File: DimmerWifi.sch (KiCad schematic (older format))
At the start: 13 parts, among them J1 AC, J2 Load, J3 Conn_01x04, U1 MOC3021M, U2 4N25

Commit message: fix
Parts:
- removed D1: Q_TRIAC_AAG, TO_SOT_Packages_THT:TO-220-3_Vertical, symbol Q_TRIAC_AAG
- removed D3: LED, LEDs:LED_D5.0mm, symbol LED
- added Q1: TRIAC_BTA, w_to:to220, symbol TRIAC_BTA
- J1, J2: footprint TerminalBlocks_Phoenix:TerminalBlock_Phoenix_MPT-2.54mm_2pol -> w_conn_mkds:mkds_1,5-2
- J3: footprint Pin_Headers:Pin_Header_Angled_1x04_Pitch2.54mm -> w_pin_strip:pin_strip_2mm_4
- R1, R2, R3, R4, R5: footprint Resistors_THT:R_Axial_DIN0411_L9.9mm_D3.6mm_P7.62mm_Vertical -> w_pth_resistors:RC03
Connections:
- net Fase: now also Q1.2 (A2)
- net at U1.4: now also Q1.1 (G)
- net at J2.1 (Pin_1), R3.1: now also Q1.3 (A1)
- net at R4.2: now also J3.4 (Pin_4)
- net +3.3V renamed +3V3
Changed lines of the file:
@@
 EESchema Schematic File Version 2
+LIBS:DimmerWifi-rescue
 LIBS:power
 LIBS:device
@@
 LIBS:contrib
 LIBS:valves
+LIBS:w_analog
+LIBS:w_connectors
+LIBS:w_device
+LIBS:w_logic
+LIBS:w_memory
+LIBS:w_microcontrollers
+LIBS:w_opto
+LIBS:w_relay
+LIBS:w_rtx
+LIBS:w_transistor
+LIBS:w_vacuum
+LIBS:DimmerWifi-cache
 EELAYER 25 0
 EELAYER END
@@
 F 0 "R1" V 2680 2000 50  0000 C CNN
 F 1 "30k" V 2600 2000 50  0000 C CNN
-F 2 "Resistors_THT:R_Axial_DIN0411_L9.9mm_D3.6mm_P7.62mm_Vertical" V 2530 2000 50  0001 C CNN
+F 2 "w_pth_resistors:RC03" V 2530 2000 50  0001 C CNN
 F 3 "" H 2600 2000 50  0001 C CNN
 	1    2600 2000
@@
 F 0 "R2" V 2680 2600 50  0000 C CNN
 F 1 "30k" V 2600 2600 50  0000 C CNN
-F 2 "Resistors_THT:R_Axial_DIN0411_L9.9mm_D3.6mm_P7.62mm_Vertical" V 2530 2600 50  0001 C CNN
+F 2 "w_pth_resistors:RC03" V 2530 2600 50  0001 C CNN
 F 3 "" H 2600 2600 50  0001 C CNN
 	1    2600 2600
@@
 F 0 "R5" V 4680 2200 50  0000 C CNN
 F 1 "3.3k" V 4600 2200 50  0000 C CNN
-F 2 "Resistors_THT:R_Axial_DIN0411_L9.9mm_D3.6mm_P7.62mm_Vertical" V 4530 2200 50  0001 C CNN
+F 2 "w_pth_resistors:RC03" V 4530 2200 50  0001 C CNN
 F 3 "" H 4600 2200 50  0001 C CNN
 	1    4600 2200
@@
 F 0 "J2" H 1500 2850 50  0000 C CNN
 F 1 "Load" H 1500 2550 50  0000 C CNN
-F 2 "TerminalBlocks_Phoenix:TerminalBlock_Phoenix_MPT-2.54mm_2pol" H 1500 2750 50  0001 C CNN
+F 2 "w_conn_mkds:mkds_1,5-2" H 1500 2750 50  0001 C CNN
 F 3 "" H 1500 2750 50  0001 C CNN
 	1    1500 2750
@@
 	1700 2300 2350 2300
 $Comp
-L +3.3V #PWR01
+L +3.3V-RESCUE-DimmerWifi #PWR01
 U 1 1 59F65F9C
 P 4600 1950
@@
 	4600 1950 4600 2050
 $Comp
-L GND #PWR02
+L GND-RESCUE-DimmerWifi #PWR02
 U 1 1 59F65FE8
 P 4550 2600
@@
 F 0 "R4" V 3780 3350 50  0000 C CNN
 F 1 "180" V 3700 3350 50  0000 C CNN
-F 2 "Resistors_THT:R_Axial_DIN0411_L9.9mm_D3.6mm_P7.62mm_Vertical" V 3630 3350 50  0001 C CNN
+F 2 "w_pth_resistors:RC03" V 3630 3350 50  0001 C CNN
 F 3 "" H 3700 3350 50  0001 C CNN
 	1    3700 3350
@@
 	3550 3350 3450 3350
 $Comp
-L GND #PWR03
+L GND-RESCUE-DimmerWifi #PWR03
 U 1 1 59F66456
 P 3500 3100
@@
 	3500 3150 3500 3100
 $Comp
-L Q_TRIAC_AAG D1
-U 1 1 59F664AA
-P 2250 3200
-F 0 "D1" H 2375 3225 50  0000 L CNN
-F 1 "Q_TRIAC_AAG" H 2375 3150 50  0000 L CNN
-F 2 "TO_SOT_Packages_THT:TO-220-3_Vertical" V 2325 3225 50  0001 C CNN
-F 3 "" V 2250 3200 50  0001 C CNN
-	1    2250 3200
-	-1   0    0    1
-$EndComp
-$Comp
 L R R3
 U 1 1 59F66521
@@
 F 0 "R3" V 2680 3350 50  0000 C CNN
 F 1 "1k" V 2600 3350 50  0000 C CNN
-F 2 "Resistors_THT:R_Axial_DIN0411_L9.9mm_D3.6mm_P7.62mm_Vertical" V 2530 3350 50  0001 C CNN
+F 2 "w_pth_resistors:RC03" V 2530 3350 50  0001 C CNN
 F 3 "" H 2600 3350 50  0001 C CNN
 	1    2600 3350
@@
 	1750 3350 2450 3350
 Wire Wire Line
-	2400 3100 2650 3100
+	2300 3100 2650 3100
 Wire Wire Line
 	2650 3100 2650 3150
@@
 F 0 "J1" H 1500 2400 50  0000 C CNN
 F 1 "AC" H 1500 2100 50  0000 C CNN
-F 2 "TerminalBlocks_Phoenix:TerminalBlock_Phoenix_MPT-2.54mm_2pol" H 1500 2300 50  0001 C CNN
+F 2 "w_conn_mkds:mkds_1,5-2" H 1500 2300 50  0001 C CNN
 F 3 "" H 1500 2300 50  0001 C CNN
 	1    1500 2300
@@
 Neutro
 Wire Wire Line
-	2250 3050 2250 2200
-Connection ~ 2250 2200
-Wire Wire Line
 	1700 2650 1750 2650
 Wire Wire Line
@@
 Wire Wire Line
 	1750 2750 1750 3350
-Connection ~ 2250 3350
 Wire Wire Line
 	2350 2000 2450 2000
@@
 F 0 "J3" H 5800 2550 50  0000 C CNN
 F 1 "Conn_01x04" H 5800 2050 50  0000 C CNN
-F 2 "Pin_Headers:Pin_Header_Angled_1x04_Pitch2.54mm" H 5800 2350 50  0001 C CNN
+F 2 "w_pin_strip:pin_strip_2mm_4" H 5800 2350 50  0001 C CNN
 F 3 "" H 5800 2350 50  0001 C CNN
 	1    5800 2350
@@
 	5600 2550 5400 2550
 Wire Wire Line
-	5400 2550 5400 3350
+	5400 3350 5400 2550
 Wire Wire Line
 	4550 2600 4550 2500
 Connection ~ 4550 2500
-$Comp
-L LED D3
-U 1 1 59F678D1
-P 4100 3350
-F 0 "D3" H 4100 3450 50  0000 C CNN
-F 1 "LED" H 4100 3250 50  0000 C CNN
-F 2 "LEDs:LED_D5.0mm" H 4100 3350 50  0001 C CNN
-F 3 "" H 4100 3350 50  0001 C CNN
-	1    4100 3350
-	1    0    0    -1
-$EndComp
-Wire Wire Line
-	3950 3350 3850 3350
-Wire Wire Line
-	5400 3350 4250 3350
+Wire Wire Line
+	3850 3350 5400 3350
 $Comp
 L PWR_FLAG #FLG04
@@
 Connection ~ 5400 2000
 NoConn ~ 4450 2300
+$Comp
+L TRIAC_BTA Q1
+U 1 1 59F8B5BD
+P 2100 3000
+F 0 "Q1" H 2200 3150 60  0000 C CNN
+F 1 "TRIAC_BTA" H 2400 2750 60  0000 C CNN
+F 2 "w_to:to220" H 2100 3000 60  0001 C CNN
+F 3 "" H 2100 3000 60  0000 C CNN
+	1    2100 3000
+	1    0    0    -1
+$EndComp
+Wire Wire Line
+	2100 2850 2100 2200
+Connection ~ 2100 2200
+Wire Wire Line
+	2100 3150 2100 3350
+Connection ~ 2100 3350
 $EndSCHEMATC

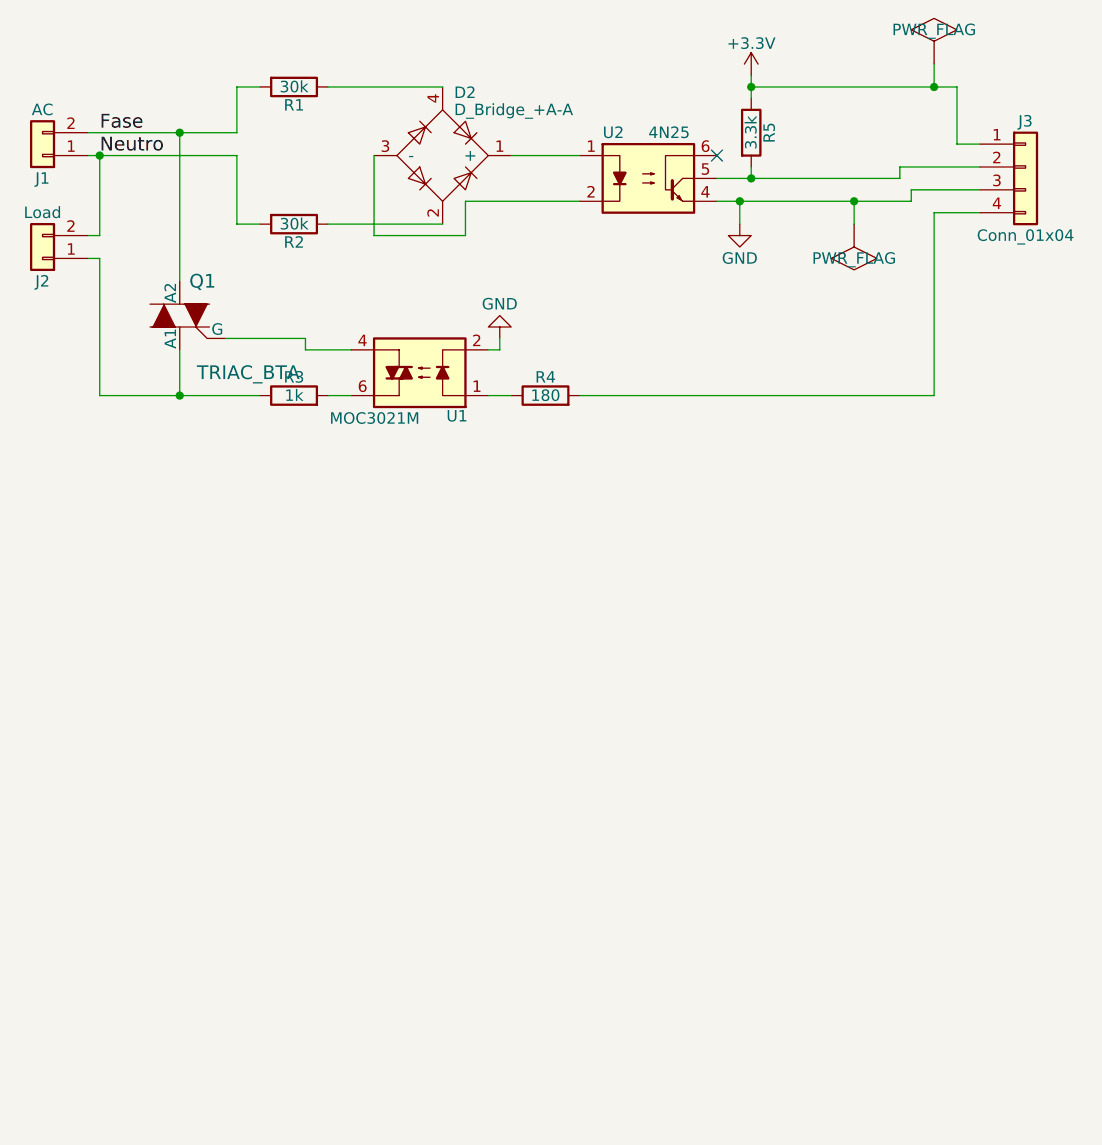
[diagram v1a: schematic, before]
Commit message: add esp32
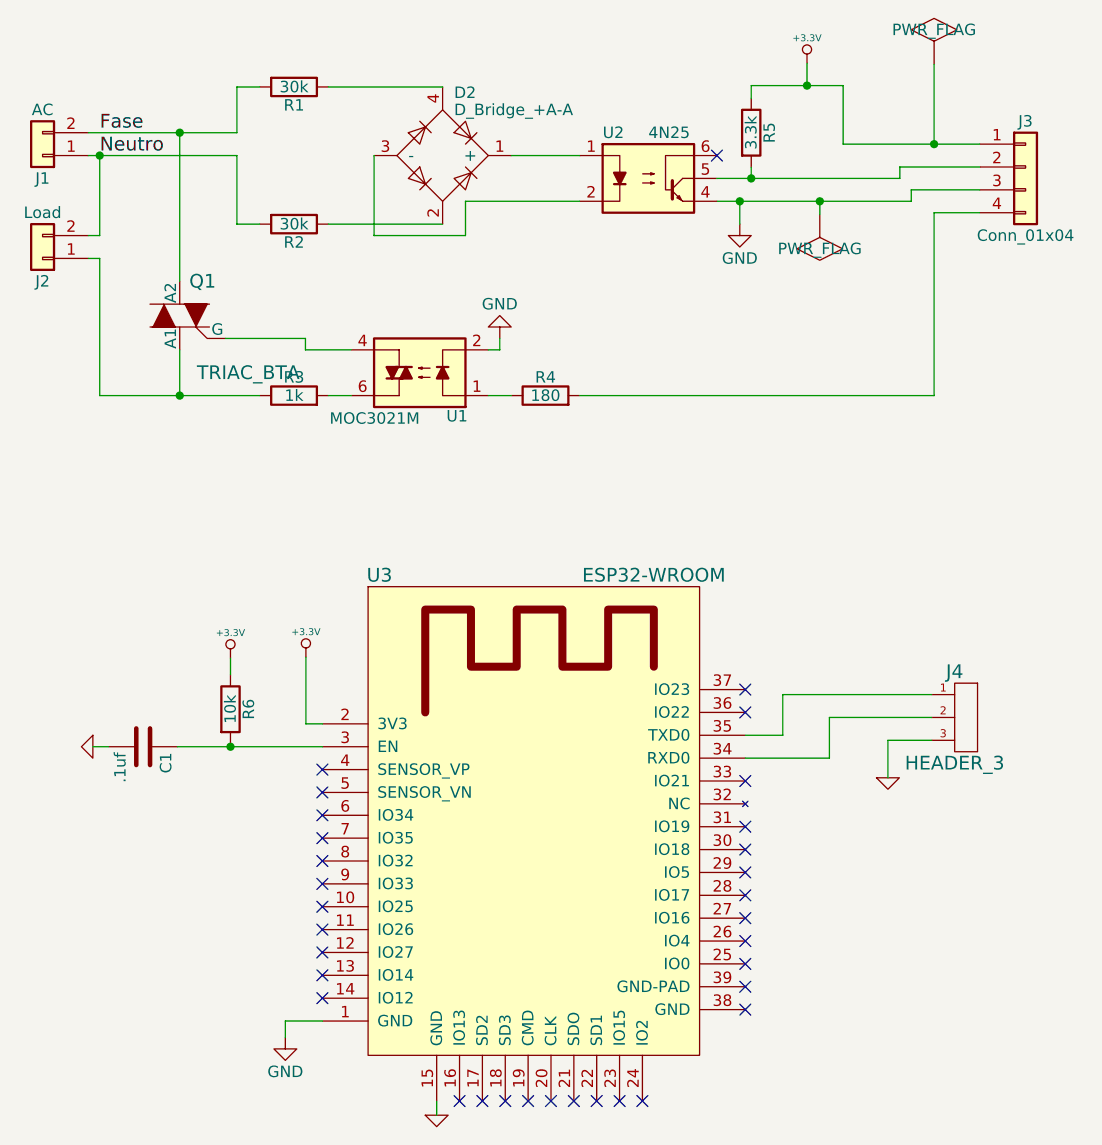
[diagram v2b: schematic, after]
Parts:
- added C1: .1uf, symbol C
- added J4: HEADER_3, symbol HEADER_3
- added R6: 10k, symbol R
- added U3: ESP32-WROOM, ESP32-footprints-Lib:ESP32-WROOM, symbol ESP32-WROOM
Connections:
- net GND: now also C1.2, J4.3, U3.1 (GND), U3.15 (GND)
- net +3V3 renamed +3.3V
- net +3.3V: now also R6.1, U3.2 (3V3)
- new net: C1.1, R6.2, U3.3 (EN)
- new net: J4.2, U3.34 (RXD0)
- new net: J4.1, U3.35 (TXD0)
- no-connect marks 1 -> 33
